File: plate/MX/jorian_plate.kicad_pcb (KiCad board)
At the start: 2 copper layers, 152.4 x 85.1 mm, 29 parts, among them SW1 SW_PUSH, SW10 SW_PUSH, SW11 SW_PUSH, SW12 SW_PUSH, SW13 SW_PUSH, SW14 SW_PUSH, SW15 SW_PUSH, SW16 SW_PUSH, SW17 SW_PUSH, SW18 SW_PUSH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

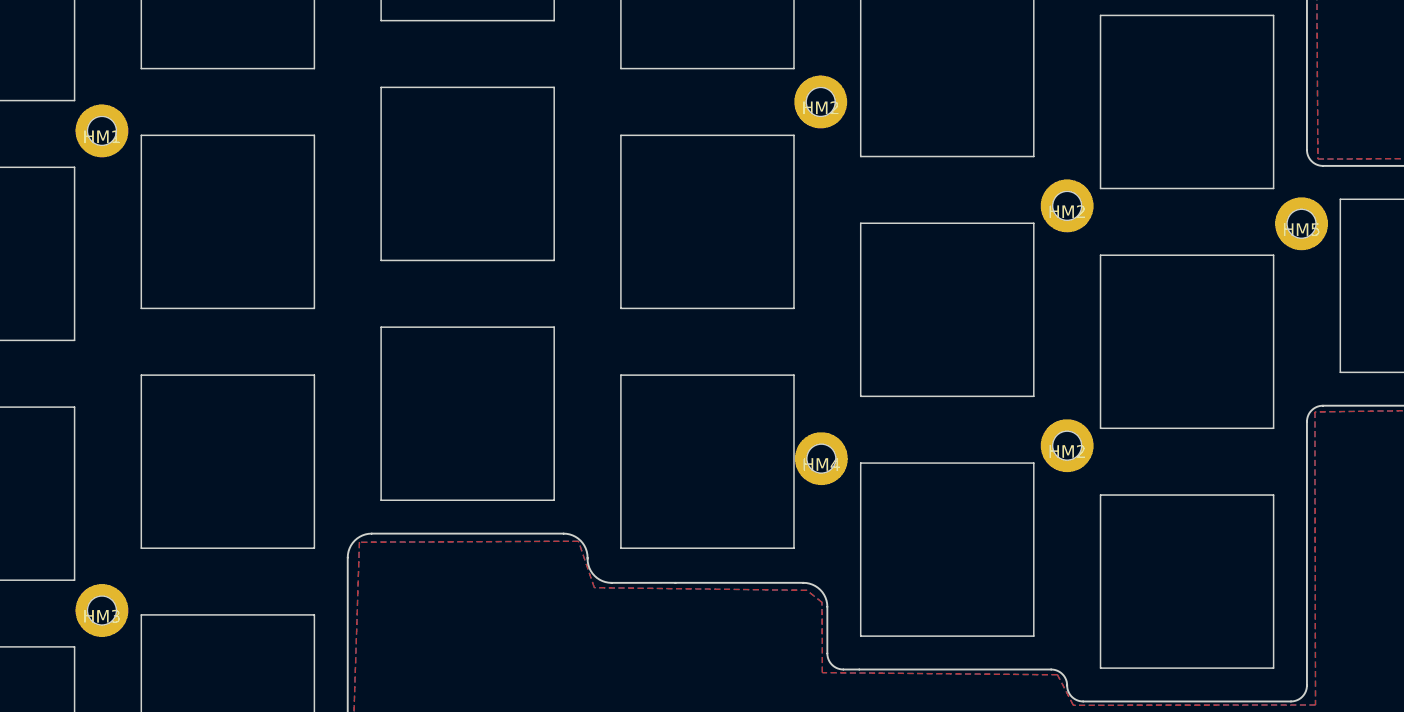
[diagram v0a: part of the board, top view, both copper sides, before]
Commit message: Updated case hole footprints
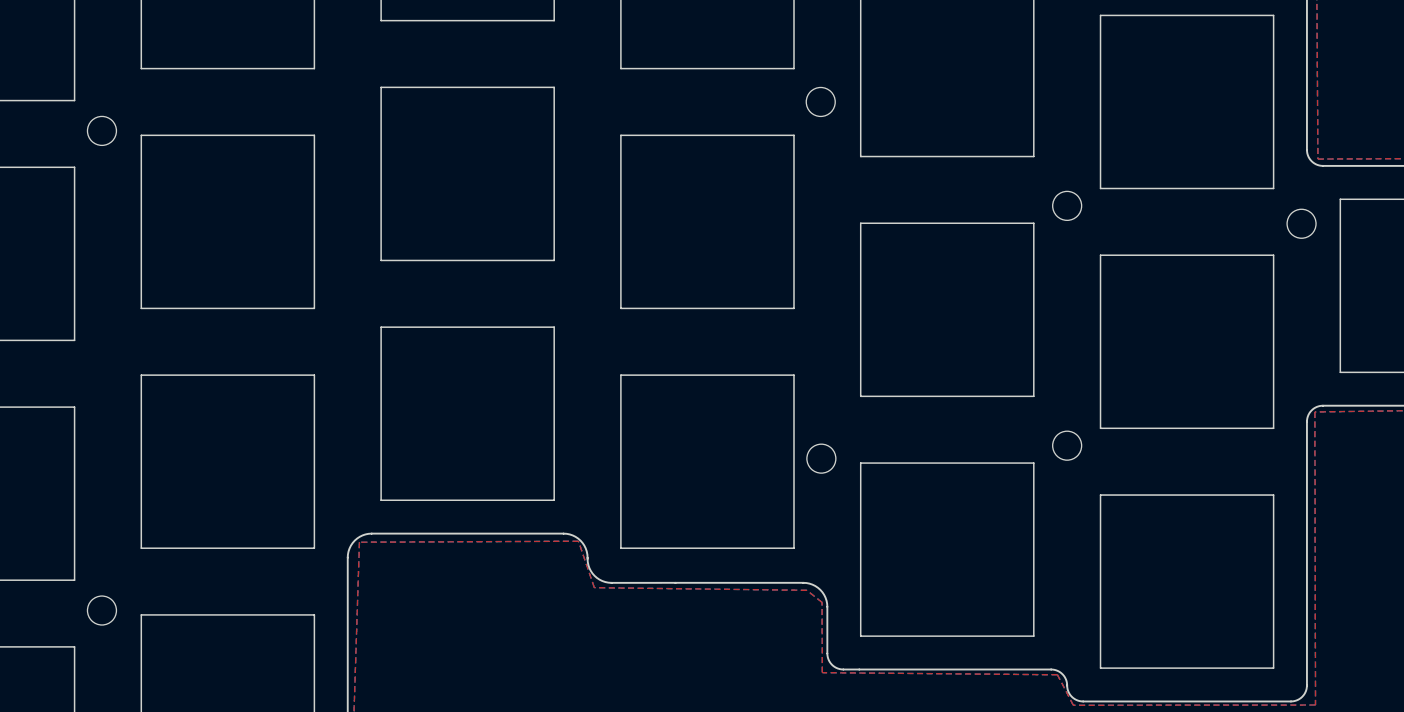
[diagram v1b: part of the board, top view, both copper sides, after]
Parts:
- HM1, HM2, HM3, HM4, HM5: footprint kbd:M2_Hole_TH_mod -> kbd:M2_Hole_Edge_Cut
- HM6, HM7: renamed from HM2; footprint kbd:M2_Hole_TH_mod -> kbd:M2_Hole_Edge_Cut
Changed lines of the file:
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@@
     (fp_line (start 9.525 -9.525) (end -9.525 -9.525) (layer "F.Fab") (width 0.15))
   )
-  (footprint "kbd:M2_Hole_TH_mod" (layer "F.Cu")
+  (footprint "kbd:M2_Hole_Edge_Cut" (layer "F.Cu")
     (at 59.85 101.995)
     (property "Sheetfile" "jorian.kicad_sch")
     (property "Sheetname" "")
-    (fp_text reference "HM3" (at 0 0.5) (layer "F.SilkS")
+    (fp_text reference "HM3" (at 0 1.9) (layer "Dwgs.User")
       (effects (font (size 1 1) (thickness 0.15)))
     )
-    (fp_text value "CaseHole" (at 0 -0.5) (layer "F.Fab")
-      (effects (font (size 1 1) (thickness 0.15)))
-    )
-    (fp_text user "${REFERENCE}" (at 0.3 0) (layer "F.Fab")
+    (fp_text value "CaseHole" (at 0 -1.8) (layer "F.Fab")
       (effects (font (size 1 1) (thickness 0.15)))
     )
     (fp_circle (center 0 0) (end 1.15 0) (layer "Edge.Cuts") (width 0.1) (fill none))
-    (pad "" thru_hole circle (at 0 0) (size 4.2 4.2) (drill 2.3) (layers *.Cu *.Mask))
   )
-  (footprint "kbd:M2_Hole_TH_mod" (layer "F.Cu")
+  (footprint "kbd:M2_Hole_Edge_Cut" (layer "F.Cu")
     (at 155.145948 71.270959)
     (property "Sheetfile" "jorian.kicad_sch")
     (property "Sheetname" "")
-    (fp_text reference "HM5" (at 0 0.5) (layer "F.SilkS")
+    (fp_text reference "HM5" (at 0 1.9) (layer "Dwgs.User")
       (effects (font (size 1 1) (thickness 0.15)))
     )
-    (fp_text value "CaseHole" (at 0 -0.5) (layer "F.Fab")
-      (effects (font (size 1 1) (thickness 0.15)))
-    )
-    (fp_text user "${REFERENCE}" (at 0.3 0) (layer "F.Fab")
+    (fp_text value "CaseHole" (at 0 -1.8) (layer "F.Fab")
       (effects (font (size 1 1) (thickness 0.15)))
     )
     (fp_circle (center 0 0) (end 1.15 0) (layer "Edge.Cuts") (width 0.1) (fill none))
-    (pad "" thru_hole circle (at 0 0) (size 4.2 4.2) (drill 2.3) (layers *.Cu *.Mask))
   )
-  (footprint "kbd:M2_Hole_TH_mod" (layer "F.Cu")
+  (footprint "kbd:M2_Hole_Edge_Cut" (layer "F.Cu")
     (at 116.95 61.595)
     (property "Sheetfile" "jorian.kicad_sch")
     (property "Sheetname" "")
-    (fp_text reference "HM2" (at 0 0.5) (layer "F.SilkS")
+    (fp_text reference "HM2" (at 0 1.9) (layer "Dwgs.User")
       (effects (font (size 1 1) (thickness 0.15)))
     )
-    (fp_text value "CaseHole" (at 0 -0.5) (layer "F.Fab")
-      (effects (font (size 1 1) (thickness 0.15)))
-    )
-    (fp_text user "${REFERENCE}" (at 0.3 0) (layer "F.Fab")
+    (fp_text value "CaseHole" (at 0 -1.8) (layer "F.Fab")
       (effects (font (size 1 1) (thickness 0.15)))
     )
     (fp_circle (center 0 0) (end 1.15 0) (layer "Edge.Cuts") (width 0.1) (fill none))
-    (pad "" thru_hole circle (at 0 0) (size 4.2 4.2) (drill 2.3) (layers *.Cu *.Mask))
   )
-  (footprint "kbd:M2_Hole_TH_mod" (layer "F.Cu")
+  (footprint "kbd:M2_Hole_Edge_Cut" (layer "F.Cu")
     (at 117 89.93)
     (property "Sheetfile" "jorian.kicad_sch")
     (property "Sheetname" "")
-    (fp_text reference "HM4" (at 0 0.5) (layer "F.SilkS")
+    (fp_text reference "HM4" (at 0 1.9) (layer "Dwgs.User")
       (effects (font (size 1 1) (thickness 0.15)))
     )
-    (fp_text value "CaseHole" (at 0 -0.5) (layer "F.Fab")
-      (effects (font (size 1 1) (thickness 0.15)))
-    )
-    (fp_text user "${REFERENCE}" (at 0.3 0) (layer "F.Fab")
+    (fp_text value "CaseHole" (at 0 -1.8) (layer "F.Fab")
       (effects (font (size 1 1) (thickness 0.15)))
     )
     (fp_circle (center 0 0) (end 1.15 0) (layer "Edge.Cuts") (width 0.1) (fill none))
-    (pad "" thru_hole circle (at 0 0) (size 4.2 4.2) (drill 2.3) (layers *.Cu *.Mask))
   )
-  (footprint "kbd:M2_Hole_TH_mod" (layer "F.Cu")
+  (footprint "kbd:M2_Hole_Edge_Cut" (layer "F.Cu")
     (at 136.525 69.85)
     (property "Sheetfile" "jorian.kicad_sch")
     (property "Sheetname" "")
-    (fp_text reference "HM2" (at 0 0.5) (layer "F.SilkS")
+    (fp_text reference "HM6" (at 0 1.9) (layer "Dwgs.User")
       (effects (font (size 1 1) (thickness 0.15)))
     )
-    (fp_text value "CaseHole" (at 0 -0.5) (layer "F.Fab")
-      (effects (font (size 1 1) (thickness 0.15)))
-    )
-    (fp_text user "${REFERENCE}" (at 0.3 0) (layer "F.Fab")
+    (fp_text value "CaseHole" (at 0 -1.8) (layer "F.Fab")
       (effects (font (size 1 1) (thickness 0.15)))
     )
     (fp_circle (center 0 0) (end 1.15 0) (layer "Edge.Cuts") (width 0.1) (fill none))
-    (pad "" thru_hole circle (at 0 0) (size 4.2 4.2) (drill 2.3) (layers *.Cu *.Mask))
   )
-  (footprint "kbd:M2_Hole_TH_mod" (layer "F.Cu")
+  (footprint "kbd:M2_Hole_Edge_Cut" (layer "F.Cu")
     (at 136.525 88.9)
     (property "Sheetfile" "jorian.kicad_sch")
     (property "Sheetname" "")
-    (fp_text reference "HM2" (at 0 0.5) (layer "F.SilkS")
+    (fp_text reference "HM7" (at 0 1.9) (layer "Dwgs.User")
       (effects (font (size 1 1) (thickness 0.15)))
     )
-    (fp_text value "CaseHole" (at 0 -0.5) (layer "F.Fab")
-      (effects (font (size 1 1) (thickness 0.15)))
-    )
-    (fp_text user "${REFERENCE}" (at 0.3 0) (layer "F.Fab")
+    (fp_text value "CaseHole" (at 0 -1.8) (layer "F.Fab")
       (effects (font (size 1 1) (thickness 0.15)))
     )
     (fp_circle (center 0 0) (end 1.15 0) (layer "Edge.Cuts") (width 0.1) (fill none))
-    (pad "" thru_hole circle (at 0 0) (size 4.2 4.2) (drill 2.3) (layers *.Cu *.Mask))
   )
-  (footprint "kbd:M2_Hole_TH_mod" (layer "F.Cu")
+  (footprint "kbd:M2_Hole_Edge_Cut" (layer "F.Cu")
     (at 59.85 63.895)
     (property "Sheetfile" "jorian.kicad_sch")
     (property "Sheetname" "")
-    (fp_text reference "HM1" (at 0 0.5) (layer "F.SilkS")
+    (fp_text reference "HM1" (at 0 1.9) (layer "Dwgs.User")
       (effects (font (size 1 1) (thickness 0.15)))
     )
-    (fp_text value "CaseHole" (at 0 -0.5) (layer "F.Fab")
-      (effects (font (size 1 1) (thickness 0.15)))
-    )
-    (fp_text user "${REFERENCE}" (at 0.3 0) (layer "F.Fab")
+    (fp_text value "CaseHole" (at 0 -1.8) (layer "F.Fab")
       (effects (font (size 1 1) (thickness 0.15)))
     )
     (fp_circle (center 0 0) (end 1.15 0) (layer "Edge.Cuts") (width 0.1) (fill none))
-    (pad "" thru_hole circle (at 0 0) (size 4.2 4.2) (drill 2.3) (layers *.Cu *.Mask))
   )
   (gr_arc (start 97.155 38.735) (mid 98.053026 39.106974) (end 98.425 40.005) (layer "Edge.Cuts") (width 0.15))
